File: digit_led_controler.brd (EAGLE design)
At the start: 49.2 x 48.2 mm, 37 parts

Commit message: Update digit_led_controler.brd
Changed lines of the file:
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@@
 <layer number="1" name="Top" color="4" fill="1" visible="yes" active="yes"/>
 <layer number="16" name="Bottom" color="1" fill="1" visible="yes" active="yes"/>
-<layer number="17" name="Pads" color="2" fill="1" visible="no" active="yes"/>
-<layer number="18" name="Vias" color="2" fill="1" visible="no" active="yes"/>
+<layer number="17" name="Pads" color="2" fill="1" visible="yes" active="yes"/>
+<layer number="18" name="Vias" color="2" fill="1" visible="yes" active="yes"/>
 <layer number="19" name="Unrouted" color="6" fill="1" visible="yes" active="yes"/>
 <layer number="20" name="Dimension" color="15" fill="1" visible="yes" active="yes"/>
@@
 <text x="30.48" y="78.74" size="1.016" layer="21" rot="R90" align="bottom-right">SEG3</text>
 <text x="41.91" y="78.74" size="1.016" layer="21" rot="R90" align="bottom-right">SEG4</text>
+<hole x="47.929928125" y="80.00006875" drill="3"/>
+<hole x="47.930459375" y="31.749415625" drill="3"/>
+<hole x="-1.269315625" y="31.74995" drill="3"/>
+<hole x="-1.269871875" y="80.00006875" drill="3"/>
 </plain>
 <attributes>
@@
 <wire x1="2.54" y1="38.252" x2="2.388" y2="38.1" width="0.4064" layer="1"/>
 <wire x1="7.62" y1="53.34" x2="7.62" y2="50.8" width="0.4064" layer="1"/>
-<wire x1="7.62" y1="50.8" x2="11.43" y2="46.99" width="0" layer="19" extent="1-16"/>
-<wire x1="11.43" y1="46.99" x2="11.43" y2="43.18" width="0" layer="19" extent="1-16"/>
-<wire x1="11.43" y1="43.18" x2="10.16" y2="41.91" width="0" layer="19" extent="1-16"/>
+<wire x1="7.62" y1="50.8" x2="10.16" y2="48.26" width="0.4064" layer="1"/>
+<wire x1="10.16" y1="48.26" x2="10.16" y2="43.18" width="0.4064" layer="1"/>
+<wire x1="10.16" y1="43.18" x2="8.89" y2="41.91" width="0.4064" layer="1"/>
+<wire x1="8.89" y1="41.91" x2="8.11" y2="41.91" width="0.4064" layer="1"/>
 <wire x1="8.11" y1="41.91" x2="7.79" y2="41.59" width="0.4064" layer="1"/>
-<wire x1="8.11" y1="41.91" x2="8.89" y2="41.91" width="0.4064" layer="1"/>
-<wire x1="8.89" y1="41.91" x2="10.16" y2="43.18" width="0.4064" layer="1"/>
-<wire x1="10.16" y1="43.18" x2="10.16" y2="48.26" width="0.4064" layer="1"/>
-<wire x1="10.16" y1="48.26" x2="7.62" y2="50.8" width="0.4064" layer="1"/>
 </signal>
 <signal name="N$14">

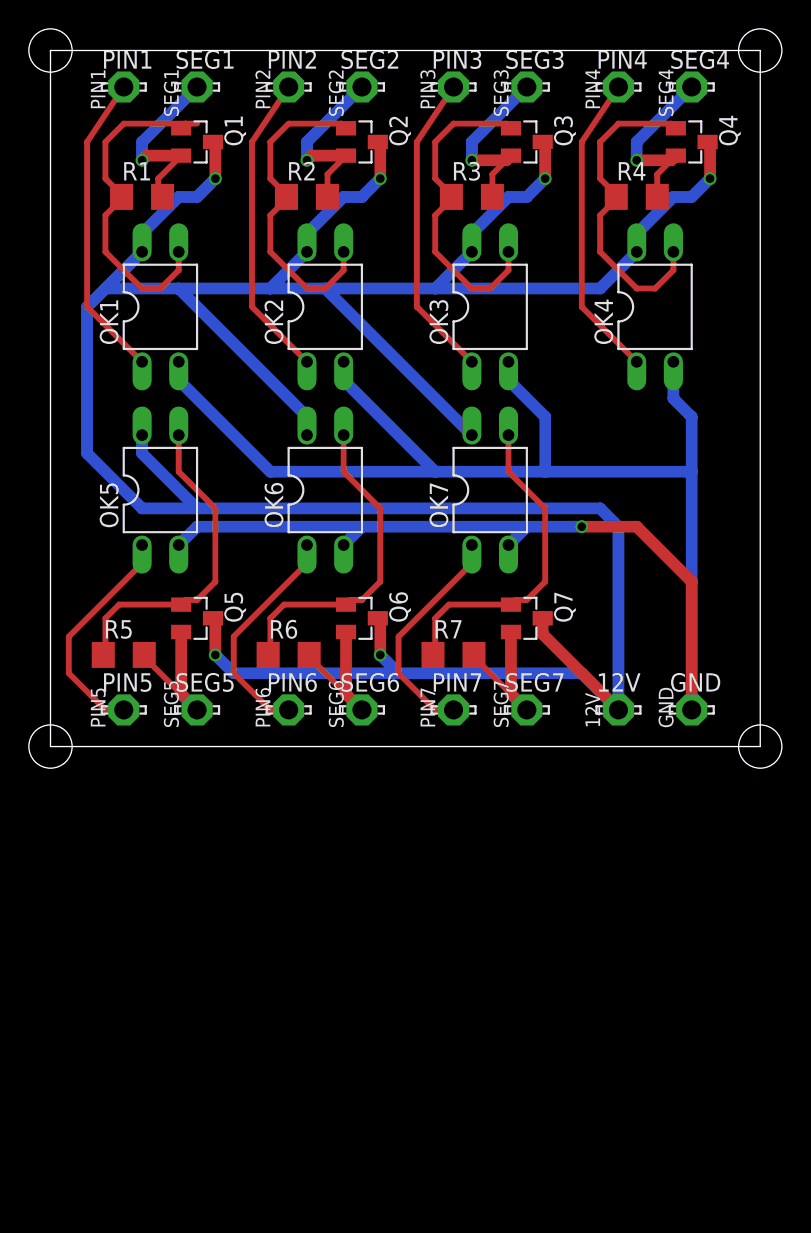
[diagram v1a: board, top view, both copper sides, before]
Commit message: Update digit_led_controler.brd
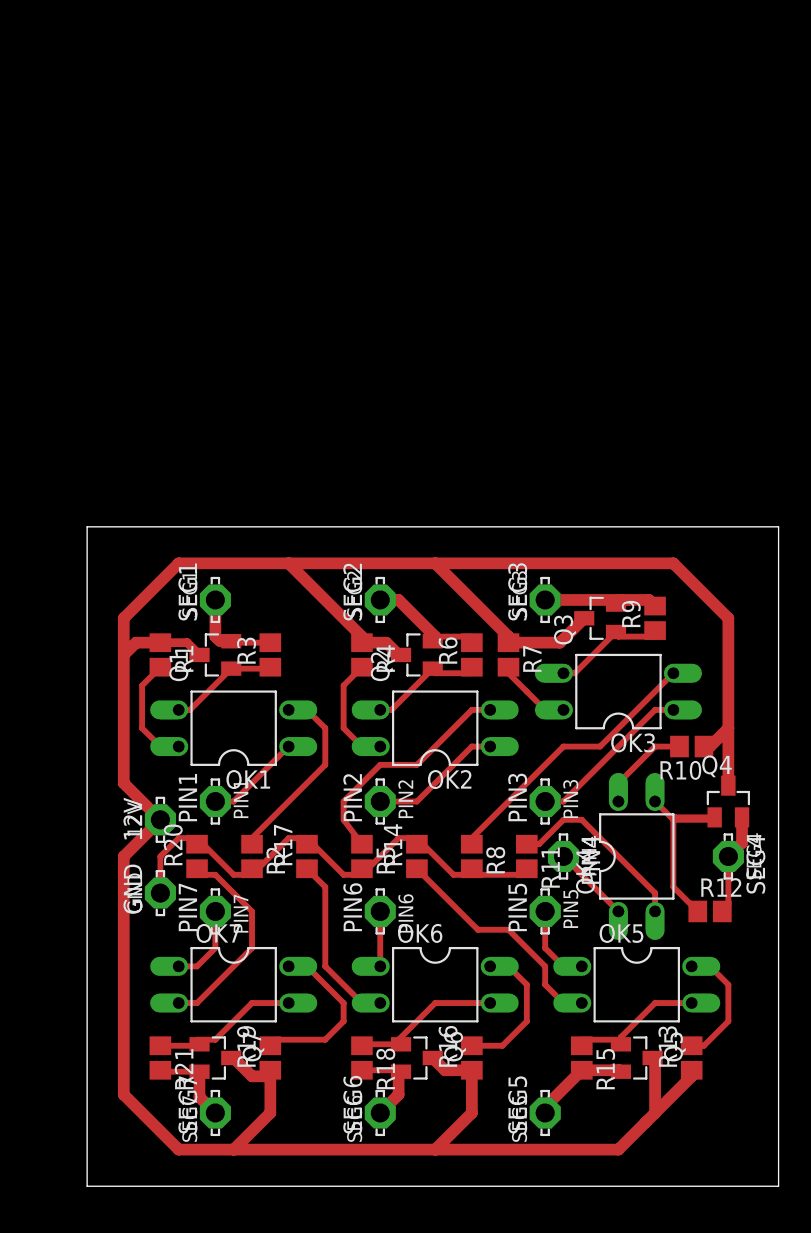
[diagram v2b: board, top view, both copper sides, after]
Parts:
- added R10, R13, R16, R19: 100, resistor:R0805
- added R11, R14, R17, R20, R8: 390, resistor:R0805
- added R12, R15, R18, R21, R9: 10000, resistor:R0805
- R1, R4, R7: value 10000 -> 100; device resistor:R1206 -> resistor:R0805
- R2, R5: value 10000 -> 390; device resistor:R1206 -> resistor:R0805
- R3, R6: device resistor:R1206 -> resistor:R0805
- moved PIN4 53.5 mm to (34.3, 24.1), turned to 270 degrees
- moved SEG4 53.4 mm to (45.7, 24.1), turned to 270 degrees
- moved PIN1 49.9 mm to (10.2, 27.9), turned to 90 degrees
- moved PIN2 49.9 mm to (21.6, 27.9), turned to 90 degrees
- moved PIN3 49.9 mm to (33.0, 27.9), turned to 90 degrees
- moved OK5 47.6 mm to (39.4, 15.2), turned to 270 degrees
- moved R2 45.9 mm to (12.7, 24.1), turned to 270 degrees
- moved Q4 45.8 mm to (45.7, 27.9), turned to 0 degrees
- moved Q5 43.1 mm to (39.4, 10.2)
- moved GND 39.0 mm to (6.35, 21.6), turned to 90 degrees
- moved OK7 38.6 mm to (11.4, 15.2), turned to 270 degrees
- moved OK4 38.1 mm to (39.4, 24.1)
- moved Q7 37.4 mm to (10.2, 10.2)
- moved R4 37.0 mm to (20.3, 38.1), turned to 270 degrees
- moved SEG5 36.9 mm to (33.0, 6.35), turned to 90 degrees
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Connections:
- removed net 12V: 12V.MP, OK1.4, OK2.4, OK3.4, OK4.4, OK5.4, OK6.4, OK7.4, Q1.3, Q2.3, Q3.3, Q4.3, Q5.3, Q6.3, Q7.3
- removed net GND: GND.MP, OK1.2, OK2.2, OK3.2, OK4.2, OK5.2, OK6.2, OK7.2
- removed net N$13 (its old number): OK5.3, Q5.1, R5.1
- removed net N$14: Q5.2, R5.2, SEG5.MP
- removed net N$19 (its old number): OK7.3, Q7.1, R7.1
- removed net N$20: Q7.2, R7.2, SEG7.MP
- removed net N$5: Q2.2, R2.2, SEG2.MP
- removed net N$7: OK3.3, Q3.1, R3.1
- new net N$12: Q2.2, R6.2, SEG2.MP
- new net N$15: OK4.4, R10.2
- new net N$18: Q3.2, R9.2, SEG3.MP
- new net N$21: OK5.4, R13.2
- new net N$22: OK4.3, Q4.1, R12.1
- new net N$23: OK6.4, R16.2
- new net N$24: Q4.2, R12.2, SEG4.MP
- new net N$27: OK1.2, R2.1
- new net N$28: OK5.3, Q5.1, R15.1
- new net N$29: OK2.2, R5.1
- new net N$30: Q5.2, R15.2, SEG5.MP
- new net N$33: OK3.2, R8.1
- new net N$34: OK6.3, Q6.1, R18.1
- new net N$35: OK4.2, R11.1
- new net N$36: Q6.2, R18.2, SEG6.MP
- new net N$39: OK5.2, R14.1
- new net N$4: Q1.2, R3.2, SEG1.MP
- new net N$40: OK7.3, Q7.1, R21.1
- new net N$41: OK6.2, R17.1
- new net N$42: Q7.2, R21.2, SEG7.MP
- new net N$44: OK7.2, R20.1
- new net N$9: GND.MP, R11.2, R14.2, R17.2, R2.2, R20.2, R5.2, R8.2
- net N$1: now also 12V.MP, Q1.3, Q2.3, Q3.3, Q4.3, Q5.3, Q6.3, Q7.3, R10.1, R13.1, R16.1, R19.1, R4.1, R7.1; no longer OK1.3, Q1.1
- net N$10: now also OK2.3, Q2.1, R6.1; no longer OK4.3, Q4.1, R4.1
- net N$11: now also OK3.4, R7.2; no longer Q4.2, R4.2, SEG4.MP
- net N$16: now also OK3.3, Q3.1, R9.1; no longer OK6.3, Q6.1, R6.1
- net N$17: now also OK7.4, R19.2; no longer Q6.2, R6.2, SEG6.MP
- net N$2: now also OK1.3, Q1.1, R3.1; no longer OK2.3, Q2.1, R2.1
- net N$3: now also OK2.4, R4.2; no longer Q1.2, R1.2, SEG1.MP
- net N$8: now also OK1.4, R1.2; no longer Q3.2, R3.2, SEG3.MP
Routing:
- net 12V: track 234.6 -> 0.00 mm, vias 6 -> 0
- net N$1: track 23.8 -> 190.9 mm
- net GND: track 133.2 -> 0.00 mm, vias 1 -> 0
- net N$9: track 0.00 -> 36.8 mm
- net N$19 (its old number): track 22.5 -> 0.00 mm
- net N$13 (its old number): track 22.5 -> 0.00 mm
- net N$7: track 22.4 -> 0.00 mm
- net N$33: track 0.00 -> 19.1 mm
- net N$29: track 0.00 -> 16.2 mm
- net N$39: track 0.00 -> 16.0 mm
- net N$25: track 21.4 -> 5.39 mm
- net N$2: track 22.6 -> 7.58 mm
- net N$6: track 21.4 -> 6.66 mm
- net N$22: track 0.00 -> 14.7 mm
- net N$10: track 22.6 -> 8.18 mm
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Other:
- board size 49.2 x 48.2 mm -> 47.9 x 45.7 mm

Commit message: Update digit_led_controler.brd
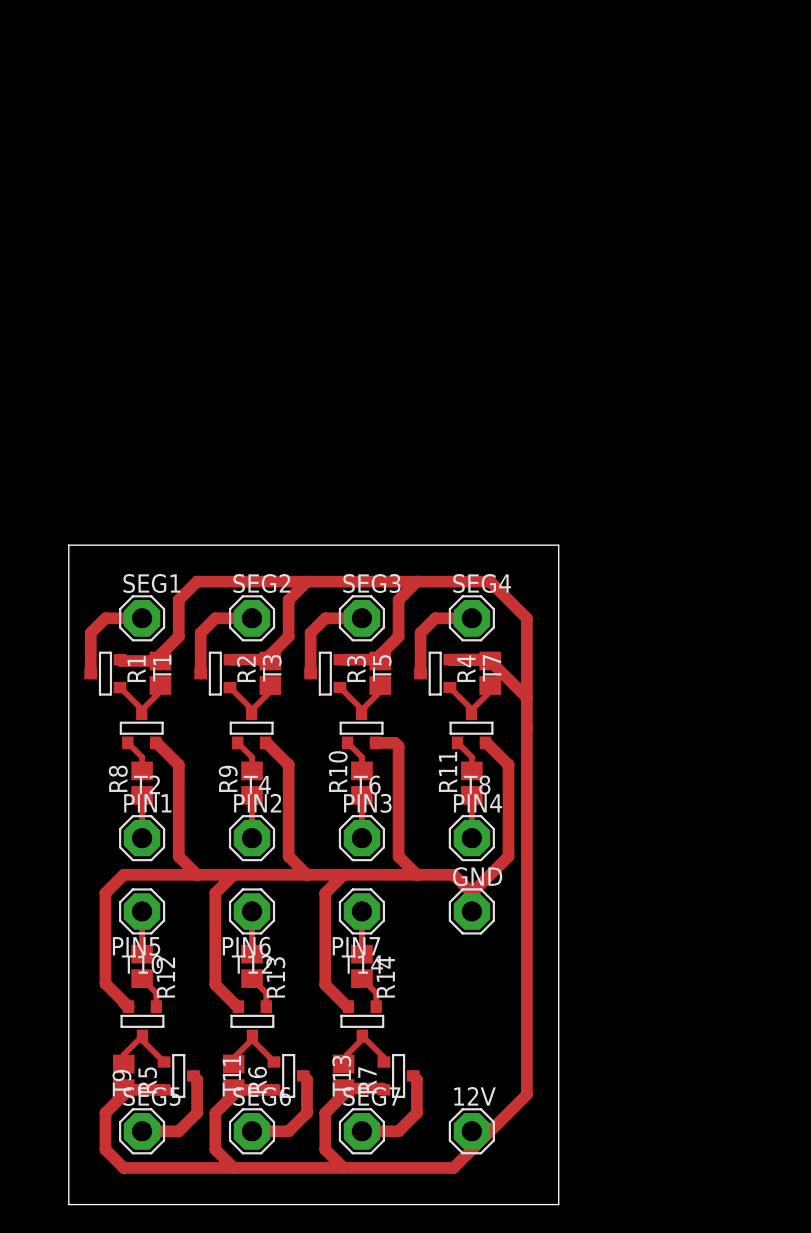
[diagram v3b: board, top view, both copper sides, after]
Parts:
- removed OK1, OK2, OK3, OK4, OK5, OK6, OK7: LTV816, optocoupler:DIL04
- removed Q1, Q2, Q3, Q4, Q5, Q6, Q7: (no value), myMOSFET:SOT23
- removed R15, R18, R21: 10000, resistor:R0805
- removed R16, R19: 100, resistor:R0805
- removed R17, R20: 390, resistor:R0805
- added T1, T10, T11, T12, T13, T14, T2, T3, T4, T5, T6, T7, T8, T9: (no value), zetex:SOT-23
- 12V, GND, PIN1, PIN2, PIN3, PIN4, PIN5, PIN6, PIN7, SEG1, SEG2, SEG3, SEG4, SEG5, SEG6, SEG7: value LSP13 -> SE14; device solpad:LSP13 -> solpad:SE14
- R1, R10, R13, R4, R7: value 100 -> (none)
- R11, R14, R2, R5, R8: value 390 -> (none)
- R12, R3, R6, R9: value 10000 -> (none)
- moved R12 39.6 mm to (5.08, 16.5), turned to 270 degrees
- moved R6 33.6 mm to (11.4, 8.89), turned to 270 degrees
- moved R7 31.4 mm to (19.1, 8.89)
- moved R13 31.1 mm to (12.7, 16.5), turned to 270 degrees
- moved 12V 30.5 mm to (27.9, 5.08), turned to 0 degrees
- moved R9 30.2 mm to (12.7, 29.2)
- moved SEG5 28.0 mm to (5.08, 5.08), turned to 0 degrees
- moved PIN5 27.9 mm to (5.08, 20.3), turned to 180 degrees
- moved SEG4 24.3 mm to (27.9, 40.6), turned to 0 degrees
- moved R8 23.4 mm to (5.08, 29.2), turned to 90 degrees
- moved R10 23.0 mm to (20.3, 29.2), turned to 90 degrees
- moved R5 22.5 mm to (3.81, 8.89)
- moved GND 21.6 mm to (27.9, 20.3), turned to 0 degrees
- moved PIN3 13.0 mm to (20.3, 25.4), turned to 0 degrees
- moved SEG3 12.8 mm to (20.3, 40.6), turned to 0 degrees
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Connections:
- removed net N$24: Q4.2, R12.2, SEG4.MP
- removed net N$25: OK4.1, PIN4.MP
- removed net N$27: OK1.2, R2.1
- removed net N$28: OK5.3, Q5.1, R15.1
- removed net N$29: OK2.2, R5.1
- removed net N$30: Q5.2, R15.2, SEG5.MP
- removed net N$31: OK5.1, PIN5.MP
- removed net N$34: OK6.3, Q6.1, R18.1
- removed net N$35: OK4.2, R11.1
- removed net N$36: Q6.2, R18.2, SEG6.MP
- removed net N$39: OK5.2, R14.1
- removed net N$40: OK7.3, Q7.1, R21.1
- removed net N$41: OK6.2, R17.1
- removed net N$42: Q7.2, R21.2, SEG7.MP
- removed net N$43: OK7.1, PIN7.MP
- removed net N$44: OK7.2, R20.1
- new net N$14: PIN7.MP, R14.1
- new net N$20: R12.2, T10.3
- new net N$26: SEG4.MP, T7.1
- new net N$46: R6.1, T11.3, T12.1
- new net N$5: R2.1, T3.3, T4.1
- new net N$50: SEG6.MP, T11.1
- new net N$61: R7.1, T13.3, T14.1
- new net N$65: SEG7.MP, T13.1
- new net N$7: PIN2.MP, R9.1
- net N$1: now also PIN1.MP, R8.1; no longer 12V.MP, Q1.3, Q2.3, Q3.3, Q4.3, Q5.3, Q6.3, Q7.3, R1.1, R10.1, R13.1, R16.1, R19.1, R4.1, R7.1
- net N$10: now also SEG2.MP, T3.1; no longer OK2.3, Q2.1, R6.1
- net N$11: now also PIN5.MP, R12.1; no longer OK3.4, R7.2
- net N$12: now also PIN6.MP, R13.1; no longer Q2.2, R6.2, SEG2.MP
- net N$13: now also R3.1, T5.3, T6.1; no longer OK2.1, PIN2.MP
- net N$15: now also R8.2, T2.3; no longer OK4.4, R10.2
- net N$16: now also R9.2, T4.3; no longer OK3.3, Q3.1, R9.1
- net N$17: now also SEG3.MP, T5.1; no longer OK7.4, R19.2
- net N$18: now also R10.2, T6.3; no longer Q3.2, R9.2, SEG3.MP
- net N$19: now also R11.2, T8.3; no longer OK3.1, PIN3.MP
- net N$2: now also R1.1, T1.3, T2.1; no longer OK1.3, Q1.1, R3.1
- net N$21: now also T12.3; no longer OK5.4
- net N$22: now also R4.1, T7.3, T8.1; no longer OK4.3, Q4.1, R12.1
- net N$23: now also R14.2, T14.3; no longer OK6.4, R16.2
- net N$3: now also GND.MP, T10.2, T12.2, T14.2, T2.2, T4.2, T6.2, T8.2; no longer OK2.4, R4.2
- net N$33: now also R5.1, T10.1, T9.3; no longer OK3.2, R8.1
- net N$37: now also SEG5.MP, T9.1; no longer OK6.1, PIN6.MP
- net N$4: now also T1.1; no longer Q1.2, R3.2
- net N$6: now also 12V.MP, R1.2, R2.2, R3.2, R4.2, R5.2, R6.2, R7.2, T1.2, T11.2, T13.2, T3.2, T5.2, T7.2, T9.2; no longer OK1.1, PIN1.MP
- net N$8: now also PIN3.MP, R10.1; no longer OK1.4, R1.2
- net N$9: now also PIN4.MP, R11.1; no longer GND.MP, R11.2, R14.2, R17.2, R2.2, R20.2, R5.2, R8.2
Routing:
- net N$1: track 190.9 -> 2.96 mm
- net N$6: track 6.66 -> 154.1 mm
- net N$3: track 7.82 -> 101.5 mm
- net N$9: track 36.8 -> 2.96 mm
- net N$29: track 16.2 -> 0.00 mm
- net N$39: track 16.0 -> 0.00 mm
- net N$44: track 14.2 -> 0.00 mm
- net N$33: track 19.1 -> 4.90 mm
- net N$27: track 13.2 -> 0.00 mm
- net N$35: track 13.0 -> 0.00 mm
- net N$41: track 12.2 -> 0.00 mm
- net N$34: track 10.5 -> 0.00 mm
- net N$40: track 10.5 -> 0.00 mm
- net N$22: track 14.7 -> 4.90 mm
- net N$28: track 9.64 -> 0.00 mm
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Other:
- board size 47.9 x 45.7 mm -> 34 x 45.7 mm
- board text removed: "12V"
- board text removed: "GND"
- board text removed: "PIN1"
- board text removed: "PIN2"
- board text removed: "PIN3"
- board text removed: "PIN4"
- board text removed: "PIN5"
- board text removed: "PIN6"
- board text removed: "PIN7"
- board text removed: "SEG1"
- board text removed: "SEG2"
- board text removed: "SEG3"
- board text removed: "SEG4"
- board text removed: "SEG5"
- board text removed: "SEG6"
- board text removed: "SEG7"
